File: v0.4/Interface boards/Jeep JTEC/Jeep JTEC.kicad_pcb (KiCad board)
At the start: 2 copper layers, 225 x 75 mm, 39 parts, among them J1 Conn_02x20_Counter_Clockwise, Q1 AO3400, Q2 IRF7317, Q3 IRF540NPBF, Q4 IRF540NPBF, Q5 IRF540NPBF, Q6 IRF540NPBF, Q7 IRF540NPBF, Q8 IRF540NPBF, U1 LM2903, U2 USBLC6-2P6

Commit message: Add 12v output to PCB
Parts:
- added H1: MountingHole, MountingHole:MountingHole_4.3mm_M4_Pad_Via, F.Cu at (120.0, 106.0)
- added H2: MountingHole, MountingHole:MountingHole_4.3mm_M4_Pad_Via, F.Cu at (48.0, 106.0)
- added H3: MountingHole, MountingHole:MountingHole_4.3mm_M4_Pad_Via, F.Cu at (120.0, 72.0)
- added H4: MountingHole, MountingHole:MountingHole_4.3mm_M4_Pad_Via, F.Cu at (48.0, 72.0)
- added H5: MountingHole, MountingHole:MountingHole_4.3mm_M4_Pad_Via, F.Cu at (192.0, 72.0)
- added H6: MountingHole, MountingHole:MountingHole_4.3mm_M4_Pad_Via, F.Cu at (192.0, 106.0)
- added J2: 12v SW Output, Connector_Phoenix_MC:PhoenixContact_MCV_1,5_2-GF-3.81_1x02_P3.81mm_Vertical_ThreadedFlange_MountHole, F.Cu at (45.0, 124.0)
- added JP3: NO, Connector_PinHeader_2.54mm:PinHeader_1x02_P2.54mm_Vertical, F.Cu at (61.0, 125.0)
- U2: value USBLC6-2P6 -> USBLC6-2SC6
- moved C4 45.0 mm to (216.0, 115.0)
- moved C5 45.0 mm to (224.0, 115.0)
- moved C6 45.0 mm to (235.0, 115.0)
- moved JP1 45.0 mm to (231.2, 121.7)
- moved JP2 45.0 mm to (226.5, 121.7)
- moved Q1 45.0 mm to (199.0, 125.0)
- moved Q2 45.0 mm to (208.0, 122.0)
- moved R1 45.0 mm to (200.0, 115.0)
- moved R10 45.0 mm to (247.0, 115.0)
- moved R11 45.0 mm to (240.0, 124.0)
- moved R2 45.0 mm to (199.0, 120.0)
- moved R3 45.0 mm to (204.0, 115.0)
- moved R4 45.0 mm to (208.0, 115.0)
- moved R6 45.0 mm to (212.0, 115.0)
- moved R7 45.0 mm to (240.0, 120.0)
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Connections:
- C1 pad 2: (no net) -> 12V-SW
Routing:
- net ASD_COIL_OUT: track 275.4 -> 334.2 mm, vias 0 -> 3
- net /CCD Decoder/CCD_TX: track 95.6 -> 43.1 mm, vias 0 -> 3
- net 12V-SW: track 0.00 -> 41.9 mm
- net CCD-: track 48.1 -> 88.5 mm, vias 0 -> 2
- net /CCD Decoder/CCD_RX: track 84.2 -> 48.7 mm, vias 1 -> 2
- net CCD+: track 33.3 -> 66.8 mm, vias 0 -> 3
- net Net-(A1-Pad22): track 31.9 -> 58.6 mm, vias 0 -> 1
- net BRAKE_LAMP_SWITCH: track 97.0 -> 121.8 mm
- net ASD_12V_IN: track 119.2 -> 143.5 mm
- net Net-(R8-Pad2): track 27.3 -> 11.1 mm
- net CRUISE_VAC_OUT: track 115.3 -> 127.9 mm, vias 1 -> 0
- net INJ-1-OUT: track 62.6 -> 50.7 mm
- net STEP-B2: track 73.8 -> 62.1 mm, vias 0 -> 1
- net GENERATOR_GND: track 173.2 -> 184.2 mm, vias 2 -> 3
- net IGN-2-DRIVER: track 140.4 -> 150.1 mm
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- added copper zone on B.Cu, net GNDA
- removed copper zone on B.Cu, net ASD_COIL_OUT

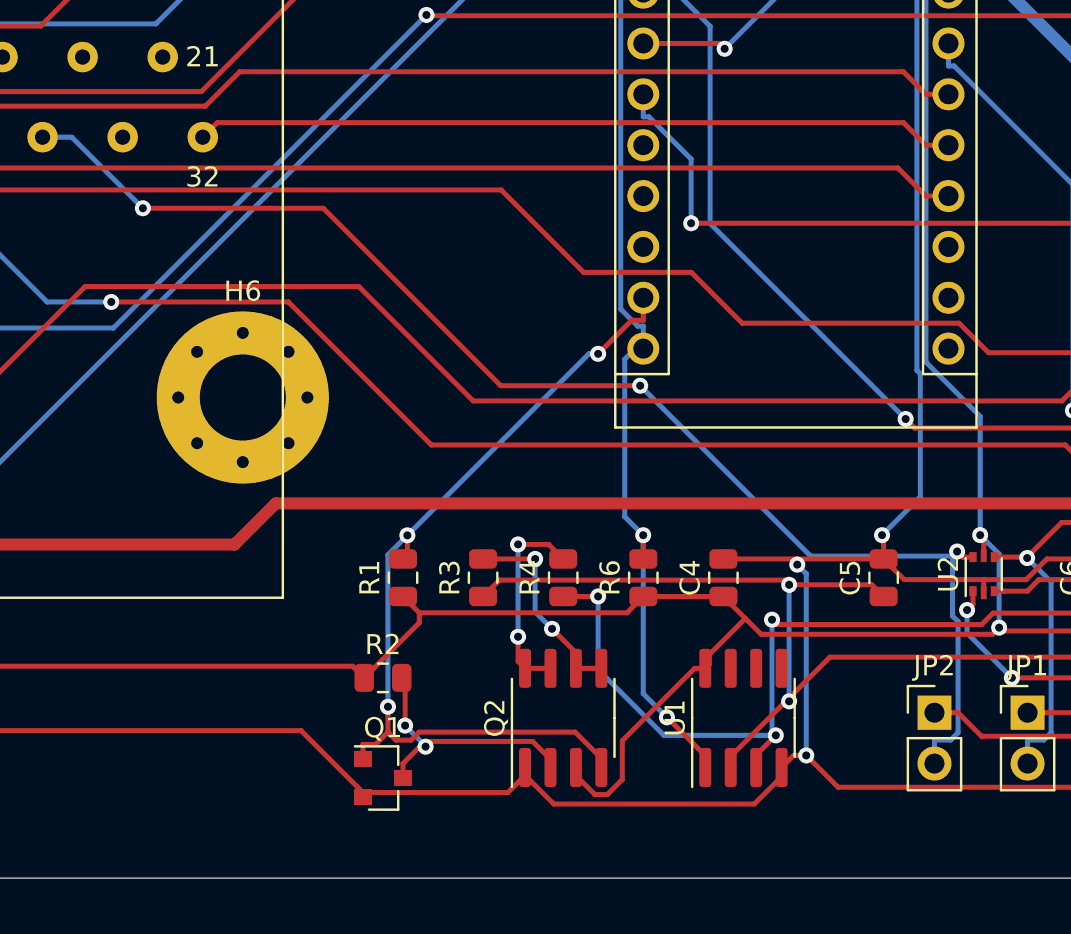
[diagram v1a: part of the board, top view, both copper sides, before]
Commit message: Add pull up resistor to cruise control input
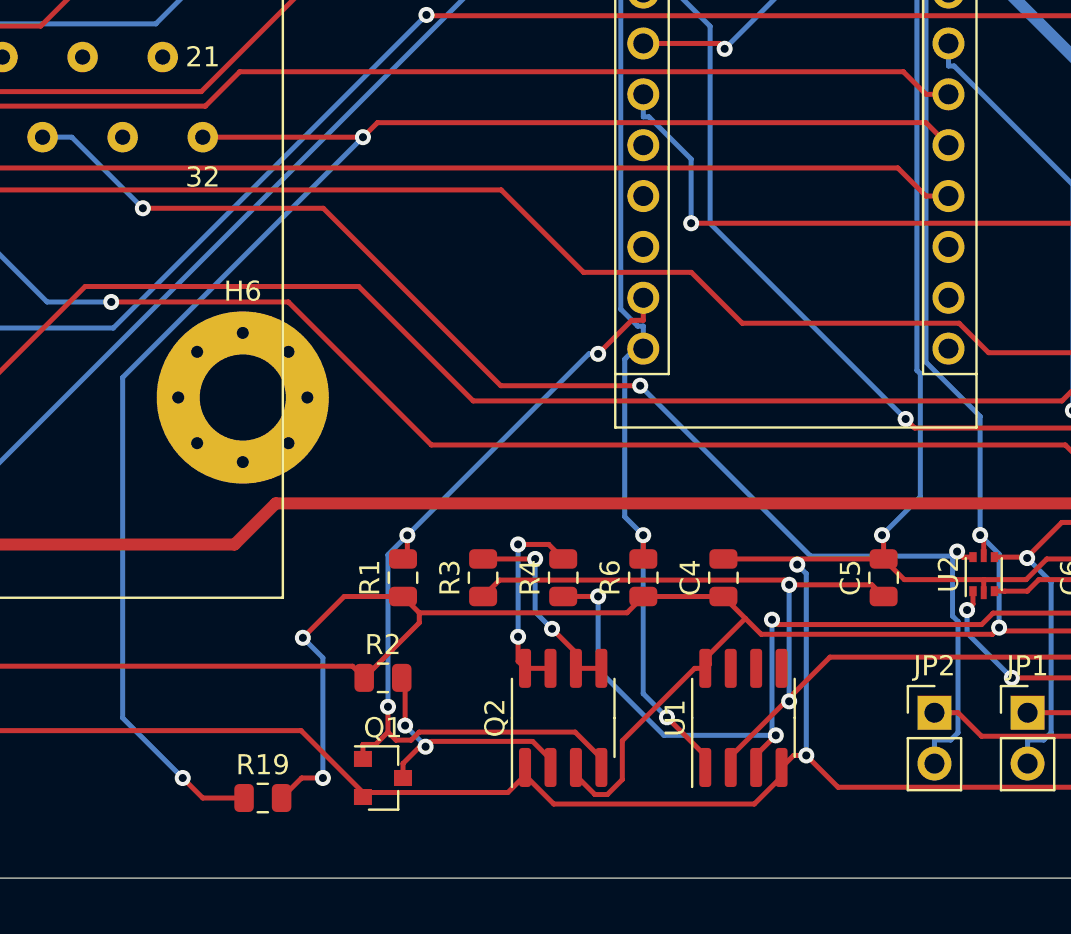
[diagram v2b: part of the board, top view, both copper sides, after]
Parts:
- added R19: 10k, Resistor_SMD:R_0805_2012Metric, F.Cu at (193.0, 126.0)
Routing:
- net SPEED_CONTROL_SWITCH: track 38.0 -> 79.7 mm, vias 0 -> 2
- net VDDA: track 287.7 -> 303.5 mm, vias 3 -> 5

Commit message: Add BOM and gerbers
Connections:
- A1 pad 23: (no net) -> CLT_Sensor
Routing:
- net CLT_Sensor: track 94.3 -> 217.7 mm, vias 1 -> 4
- net /CCD Decoder/CCD_TX: track 43.1 -> 42.5 mm
- net CCD+: track 66.8 -> 67.4 mm

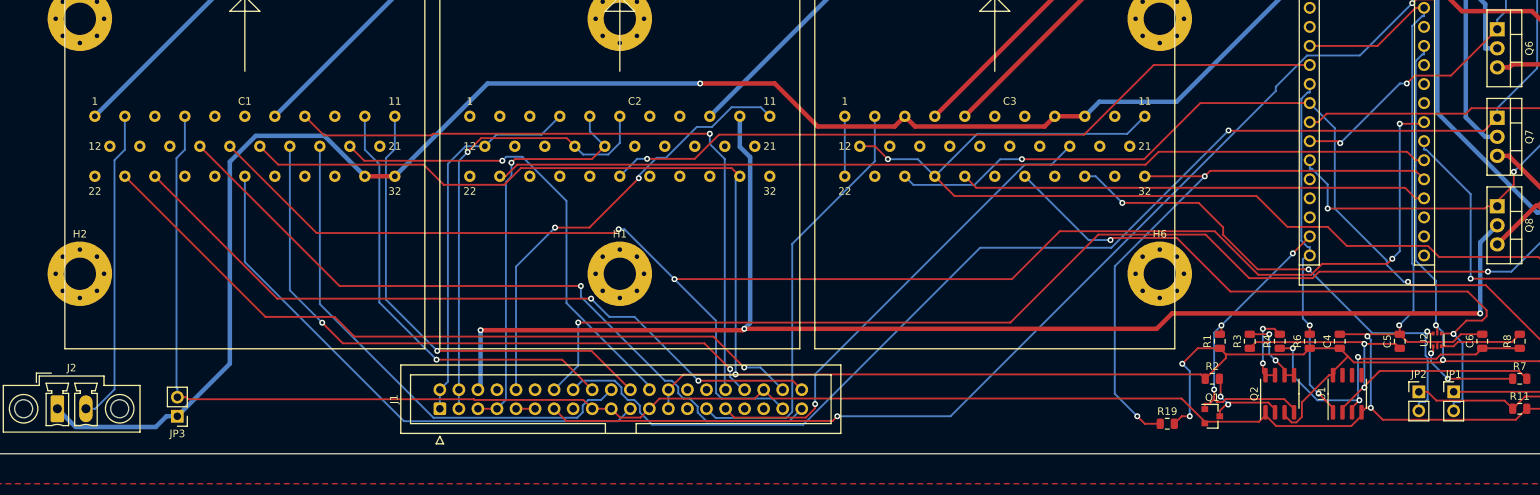
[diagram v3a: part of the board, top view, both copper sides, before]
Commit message: Correct the footprint for U2
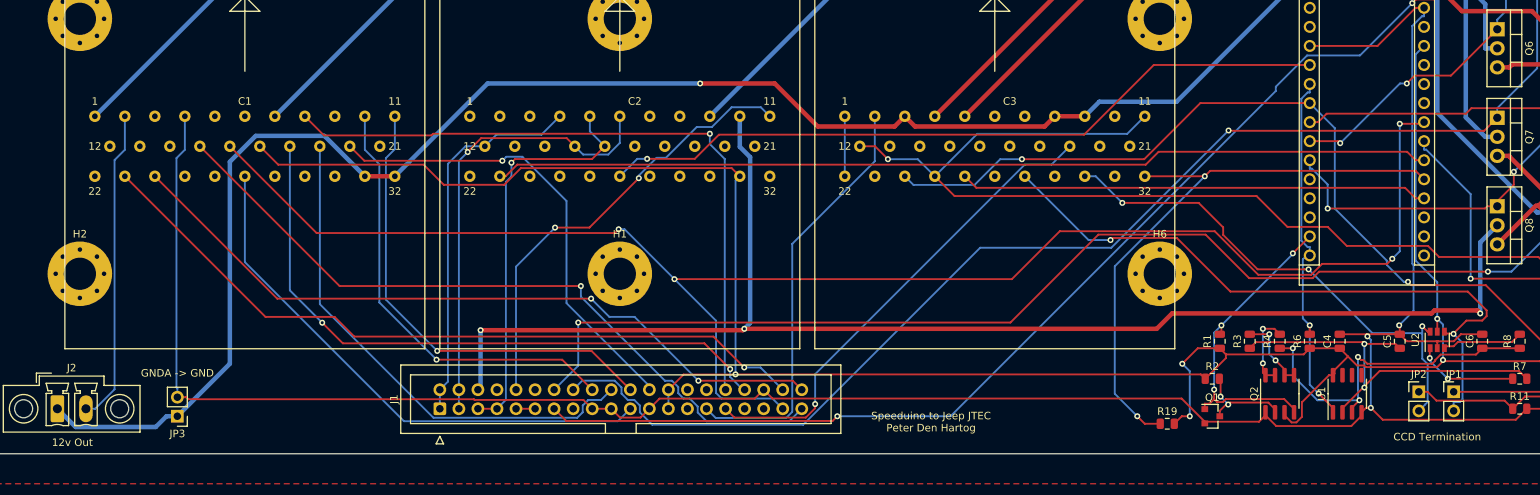
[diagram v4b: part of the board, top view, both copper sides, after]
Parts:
- U2: footprint Package_TO_SOT_SMD:SOT-666 -> Package_TO_SOT_SMD:SOT-23-6
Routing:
- net VDDA: track 303.5 -> 304.7 mm
- net /CCD Decoder/CCD_SAFE-: track 45.7 -> 46.4 mm
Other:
- board text added: "12v Out"
- board text added: "CCD Termination"
- board text added: "GNDA -> GND"
- board text added: "Speeduino to Jeep JTEC Peter Den Hartog"

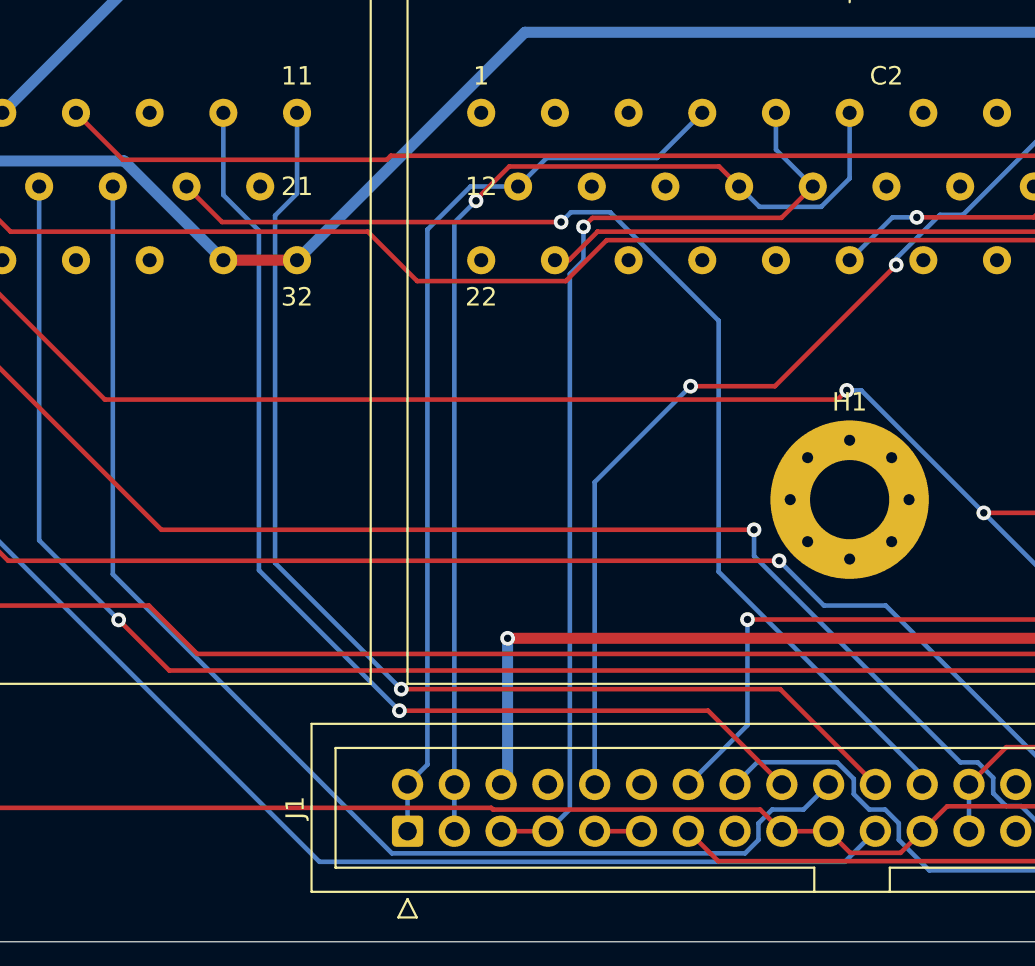
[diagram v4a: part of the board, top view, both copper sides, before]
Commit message: Correct stepper IAC phases
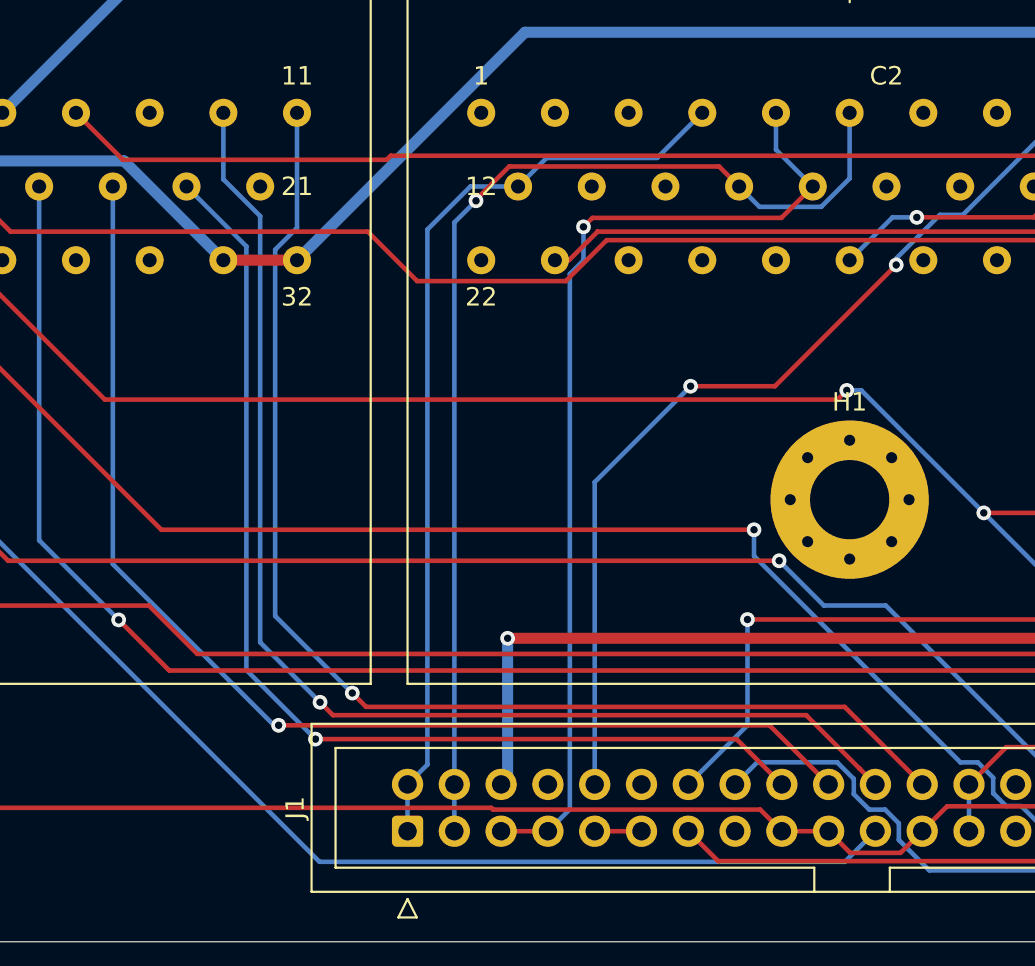
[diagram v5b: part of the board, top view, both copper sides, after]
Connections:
- C1 pad 10: STEP-A2 -> STEP-B1
- C1 pad 11: STEP-B1 -> STEP-B2
- C1 pad 20: STEP-B2 -> STEP-A2
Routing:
- net STEP-B2: track 62.1 -> 66.7 mm
- net STEP-A1: track 68.3 -> 64.3 mm, vias 0 -> 1
- net STEP-B1: track 62.5 -> 66.2 mm

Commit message: Add diodes to igniter circuit to allow ringing
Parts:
- added D2: D_Schottky 200v, Diode_SMD:D_SMB, F.Cu at (239.0, 106.0)
- added D3: D_Schottky 200v, Diode_SMD:D_SMB, F.Cu at (245.6, 106.0)
- added D4: D_Schottky 200v, Diode_SMD:D_SMB, F.Cu at (252.0, 106.0)
- moved C4 7.00 mm to (223.0, 115.0)
- moved R1 7.00 mm to (207.0, 115.0)
- moved R3 7.00 mm to (211.0, 115.0)
- moved R4 7.00 mm to (215.0, 115.0)
- moved R6 7.00 mm to (219.0, 115.0)
- moved Q3 6.40 mm to (252.0, 68.0)
- moved Q4 6.40 mm to (252.0, 79.8)
- moved Q5 6.40 mm to (252.0, 91.6)
- moved Q6 6.40 mm to (241.0, 68.4)
- moved Q7 6.40 mm to (241.0, 80.2)
- moved Q8 6.40 mm to (241.0, 92.0)
- moved R12 6.40 mm to (236.0, 60.0)
- moved R13 6.40 mm to (240.0, 60.0)
- moved R14 6.40 mm to (256.0, 60.0)
- moved R15 6.40 mm to (243.9, 60.0)
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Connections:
- Q3 pad 2: IGN-1-DRIVER -> Net-(D2-Pad1)
- Q5 pad 2: IGN-2-DRIVER -> Net-(D3-Pad1)
- Q7 pad 2: IGN-3-DRIVER -> Net-(D4-Pad1)
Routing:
- net Net-(D2-Pad1): track 0.00 -> 50.2 mm, vias 0 -> 2
- net Net-(D4-Pad1): track 0.00 -> 40.2 mm
- net IGN-1-OUT: track 166.2 -> 198.9 mm, vias 2 -> 1
- net IGN-2-DRIVER: track 150.1 -> 122.4 mm, vias 1 -> 2
- net Net-(D3-Pad1): track 0.00 -> 21.3 mm
- net ASD_12V_IN: track 143.5 -> 125.5 mm
- net BRAKE_LAMP_SWITCH: track 122.0 -> 140.0 mm
- net CCD+: track 67.6 -> 81.2 mm, vias 3 -> 1
- net IGN-1-DRIVER: track 190.0 -> 176.7 mm, vias 1 -> 2
- net Net-(A1-Pad22): track 58.6 -> 71.7 mm
- net GNDA: track 323.7 -> 336.7 mm, vias 3 -> 2
- net GENERATOR_GND: track 184.6 -> 171.5 mm, vias 3 -> 4
- net VSS: track 98.1 -> 108.5 mm, vias 1 -> 0
- net CRUISE_VAC_OUT: track 127.9 -> 118.6 mm, vias 0 -> 1
- net CLT_Sensor: track 217.7 -> 208.7 mm, vias 4 -> 2
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- added copper zone on B.Cu, net ASD_COIL_OUT
- added copper zone on F.Cu, net GNDA
- removed copper zone on F.Cu, net ASD_COIL_OUT
- removed copper zone on B.Cu, net GNDA

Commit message: Correct drill size for JTEC connector
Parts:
- removed JP3: NO, Connector_PinHeader_2.54mm:PinHeader_1x02_P2.54mm_Vertical
- added JP4: NO, Connector_PinHeader_2.54mm:PinHeader_1x02_P2.54mm_Vertical, F.Cu at (78.0, 122.5)
- added JP5: NO, Connector_PinHeader_2.54mm:PinHeader_1x02_P2.54mm_Vertical, F.Cu at (81.7, 122.5)
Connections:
- A1 pad 29: GNDA -> ASD_COIL_OUT
- A1 pad 4: GNDA -> ASD_COIL_OUT
- C1 pad 19: STEP-A1 -> Net-(C1-Pad19)
- C1 pad 20: STEP-A2 -> Net-(C1-Pad20)
- C1 pad 4: GNDA -> ASD_COIL_OUT
- C4 pad 2: GNDA -> ASD_COIL_OUT
- C5 pad 2: GNDA -> ASD_COIL_OUT
- C6 pad 2: GNDA -> ASD_COIL_OUT
- J1 pad 17: GNDA -> ASD_COIL_OUT
- J1 pad 19: GNDA -> ASD_COIL_OUT
- J1 pad 23: GNDA -> ASD_COIL_OUT
- J1 pad 36: GNDA -> ASD_COIL_OUT
- Q1 pad 2: GNDA -> ASD_COIL_OUT
- Q2 pad 1: GNDA -> ASD_COIL_OUT
- R11 pad 2: GNDA -> ASD_COIL_OUT
- R18 pad 1: GNDA -> ASD_COIL_OUT
- U1 pad 4: GNDA -> ASD_COIL_OUT
- U2 pad 2: GNDA -> ASD_COIL_OUT
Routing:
- net GNDA: track 336.7 -> 0.00 mm, vias 2 -> 0
- net ASD_COIL_OUT: track 330.8 -> 512.6 mm, vias 3 -> 5
- net Net-(C1-Pad19): track 0.00 -> 38.0 mm
- net Net-(C1-Pad20): track 0.00 -> 34.5 mm
- net IGN-1-OUT: track 198.9 -> 179.1 mm
- net INJ-3-OUT: track 57.6 -> 76.1 mm
- net IGN-2-OUT: track 189.0 -> 206.9 mm
- net VDDA: track 305.4 -> 321.3 mm, vias 3 -> 2
- net /CCD Decoder/CCD_SAFE+: track 50.5 -> 66.2 mm, vias 2 -> 0
- net STEP-A2: track 53.0 -> 37.2 mm, vias 1 -> 0
- net INJ-2-OUT: track 64.0 -> 49.1 mm
- net CRANK-IN: track 90.3 -> 75.5 mm
- net STEP-A1: track 57.4 -> 42.8 mm, vias 1 -> 0
- net Net-(JP1-Pad1): track 34.7 -> 20.8 mm, vias 1 -> 0
- net CAM-IN: track 91.6 -> 78.6 mm, vias 0 -> 1
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- added copper zone on B.Cu, net (none)
- added copper zone on F.Cu, net ASD_COIL_OUT
- removed copper zone on B.Cu, net ASD_COIL_OUT
- removed copper zone on F.Cu, net GNDA
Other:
- board text added: "Step A1 A2"
- board text removed: "GNDA -> GND"
